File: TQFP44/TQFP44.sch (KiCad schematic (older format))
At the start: 6 parts, among them J1 Conn_01x22, J2 Conn_01x22, J3 Conn_02x22_Counter_Clockwise, J4 Conn_02x22_Counter_Clockwise, J5 Conn_02x22_Counter_Clockwise, J6 Conn_01x06

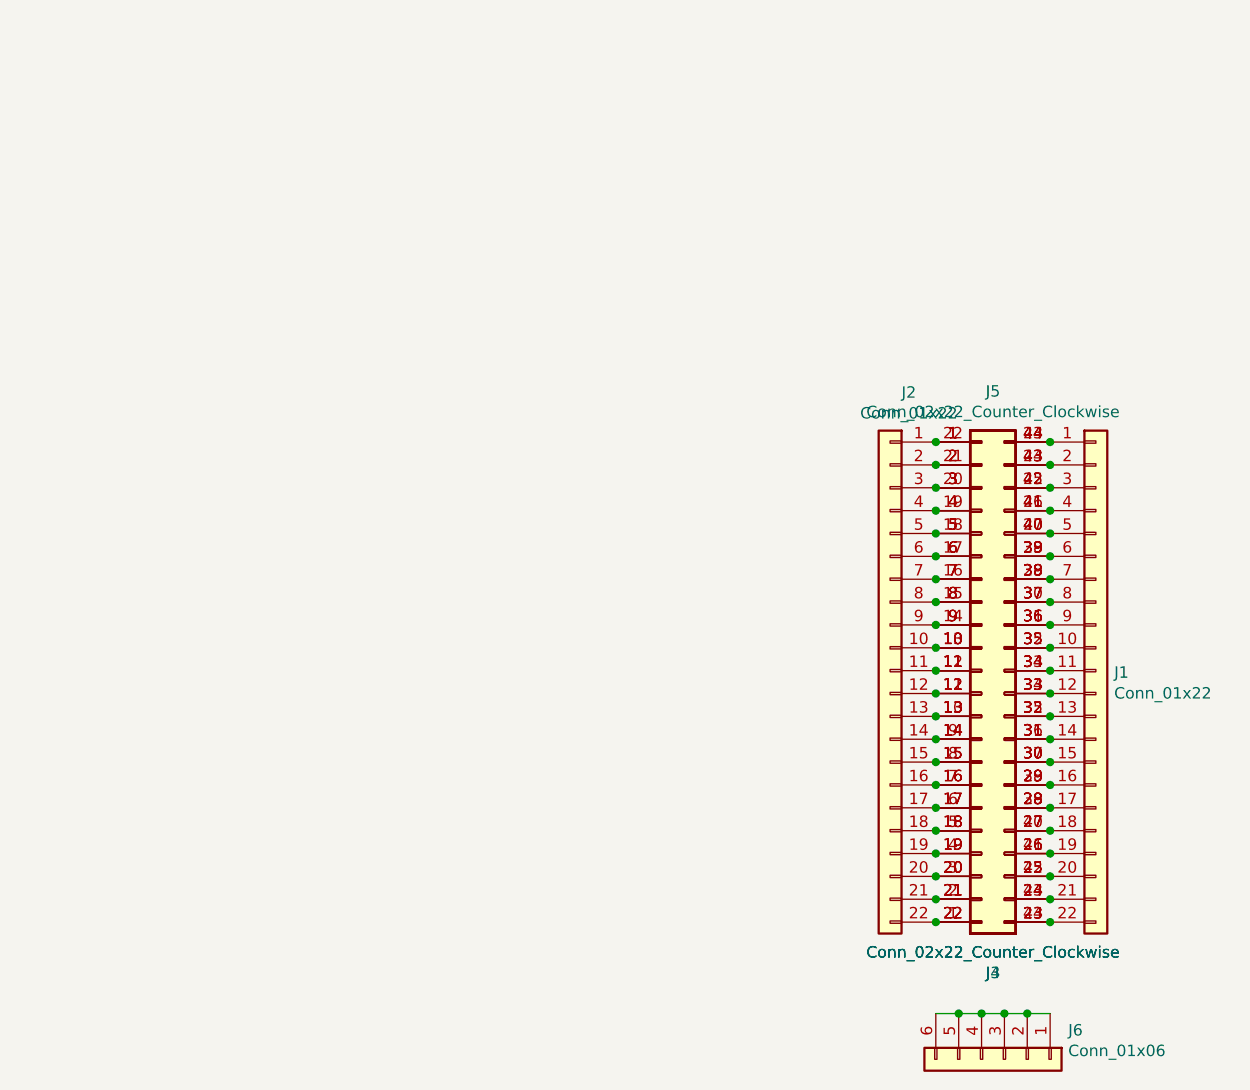
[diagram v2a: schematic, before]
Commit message: USB, SD and CR Cells Added
MicroSD, MicroUSB, MiniUSB, USB-C, CR1220, CR2032 added as well as all schematics page sizes optimised
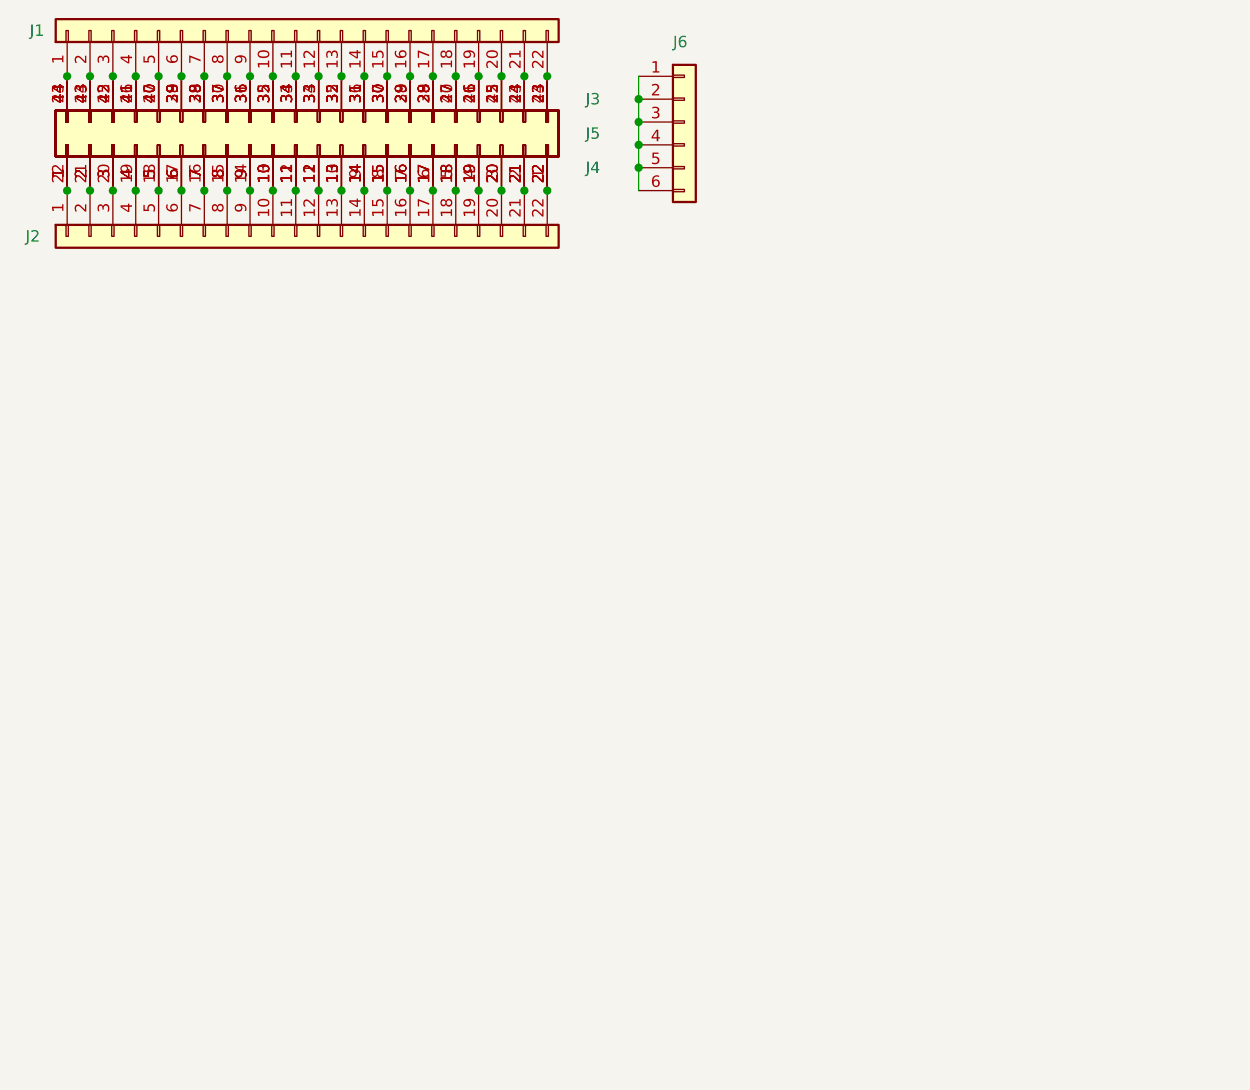
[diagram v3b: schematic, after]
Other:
- moved on the sheet: J1, J2, J3, J4, J5, J6
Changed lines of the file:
@@
 EELAYER 29 0
 EELAYER END
-$Descr A4 11693 8268
+$Descr User 5197 4016
 encoding utf-8
 Sheet 1 1
-Title ""
-Date ""
-Rev ""
-Comp ""
-Comment1 ""
-Comment2 ""
-Comment3 ""
-Comment4 ""
+Title "TQFP44 to DIP44 Breakout Board"
+Date "2019-07-04"
+Rev "1"
+Comp "SirBoard"
+Comment1 "TQFP44 P = 0.8mm"
+Comment2 "QFN44 P = 0.5mm"
+Comment3 "TSSOP44 P = 0.65mm"
+Comment4 "DIP44 P = 2.54mm"
 $EndDescr
 $Comp
 L Connector_Generic:Conn_01x22 J1
 U 1 1 5D21790C
-P 5800 3850
-F 0 "J1" H 5880 3842 50  0000 L CNN
-F 1 "Conn_01x22" H 5880 3751 50  0000 L CNN
-F 2 "Connector_PinHeader_2.54mm:PinHeader_1x22_P2.54mm_Vertical" H 5800 3850 50  0001 C CNN
-F 3 "~" H 5800 3850 50  0001 C CNN
-	1    5800 3850
-	1    0    0    -1
+P 2300 1050
+F 0 "J1" V 2300 2150 50  0000 L CNN
+F 1 "Conn_01x22" H 2380 951 50  0001 L CNN
+F 2 "Connector_PinHeader_2.54mm:PinHeader_1x22_P2.54mm_Vertical" H 2300 1050 50  0001 C CNN
+F 3 "~" H 2300 1050 50  0001 C CNN
+	1    2300 1050
+	0    -1   -1   0
 $EndComp
 $Comp
 L Connector_Generic:Conn_01x22 J2
 U 1 1 5D21CCC0
-P 4900 3850
-F 0 "J2" H 4818 5067 50  0000 C CNN
-F 1 "Conn_01x22" H 4818 4976 50  0000 C CNN
-F 2 "Connector_PinHeader_2.54mm:PinHeader_1x22_P2.54mm_Vertical" H 4900 3850 50  0001 C CNN
-F 3 "~" H 4900 3850 50  0001 C CNN
-	1    4900 3850
-	-1   0    0    -1
+P 2300 1950
+F 0 "J2" V 2300 3100 50  0000 C CNN
+F 1 "Conn_01x22" H 2218 3076 50  0001 C CNN
+F 2 "Connector_PinHeader_2.54mm:PinHeader_1x22_P2.54mm_Vertical" H 2300 1950 50  0001 C CNN
+F 3 "~" H 2300 1950 50  0001 C CNN
+	1    2300 1950
+	0    -1   1    0
 $EndComp
 $Comp
 L Connector_Generic:Conn_02x22_Counter_Clockwise J5
 U 1 1 5D30EF53
-P 5300 3950
-F 0 "J5" H 5350 2628 50  0000 C CNN
-F 1 "Conn_02x22_Counter_Clockwise" H 5350 2718 50  0000 C CNN
-F 2 "Package_QFP:TQFP-44_10x10mm_P0.8mm" H 5300 3950 50  0001 C CNN
-F 3 "~" H 5300 3950 50  0001 C CNN
-	1    5300 3950
-	1    0    0    1
+P 2400 1550
+F 0 "J5" V 2450 2750 50  0000 C CNN
+F 1 "Conn_02x22_Counter_Clockwise" H 2450 318 50  0001 C CNN
+F 2 "Package_QFP:TQFP-44_10x10mm_P0.8mm" H 2400 1550 50  0001 C CNN
+F 3 "~" H 2400 1550 50  0001 C CNN
+	1    2400 1550
+	0    1    -1   0
 $EndComp
 $Comp
 L Connector_Generic:Conn_02x22_Counter_Clockwise J3
 U 1 1 5D2DB143
-P 5300 3850
-F 0 "J3" H 5350 2528 50  0000 C CNN
-F 1 "Conn_02x22_Counter_Clockwise" H 5350 2618 50  0000 C CNN
-F 2 "Package_QFP:TQFP-44_10x10mm_P0.8mm" H 5300 3850 50  0001 C CNN
-F 3 "~" H 5300 3850 50  0001 C CNN
-	1    5300 3850
-	1    0    0    -1
+P 2300 1550
+F 0 "J3" V 2500 250 50  0000 C CNN
+F 1 "Conn_02x22_Counter_Clockwise" H 2350 318 50  0001 C CNN
+F 2 "Package_QFP:TQFP-44_10x10mm_P0.8mm" H 2300 1550 50  0001 C CNN
+F 3 "~" H 2300 1550 50  0001 C CNN
+	1    2300 1550
+	0    -1   -1   0
 $EndComp
-Connection ~ 5100 2850
-Connection ~ 5100 2950
-Connection ~ 5100 3050
-Connection ~ 5100 3150
-Connection ~ 5100 3250
-Connection ~ 5100 3350
-Connection ~ 5100 3450
-Connection ~ 5100 3550
-Connection ~ 5100 3650
-Connection ~ 5100 3750
-Connection ~ 5100 3850
-Connection ~ 5100 3950
-Connection ~ 5100 4050
-Connection ~ 5100 4150
-Connection ~ 5100 4250
-Connection ~ 5100 4350
-Connection ~ 5100 4450
-Connection ~ 5100 4550
-Connection ~ 5100 4650
-Connection ~ 5100 4750
-Connection ~ 5100 4850
-Connection ~ 5100 4950
-Connection ~ 5600 2850
-Connection ~ 5600 2950
-Connection ~ 5600 3050
-Connection ~ 5600 3150
-Connection ~ 5600 3250
-Connection ~ 5600 3350
-Connection ~ 5600 3450
-Connection ~ 5600 3550
-Connection ~ 5600 3650
-Connection ~ 5600 3750
-Connection ~ 5600 3850
-Connection ~ 5600 3950
-Connection ~ 5600 4050
-Connection ~ 5600 4150
-Connection ~ 5600 4250
-Connection ~ 5600 4350
-Connection ~ 5600 4450
-Connection ~ 5600 4550
-Connection ~ 5600 4650
-Connection ~ 5600 4750
-Connection ~ 5600 4850
-Connection ~ 5600 4950
+Connection ~ 1300 1750
+Connection ~ 1400 1750
+Connection ~ 1500 1750
+Connection ~ 1600 1750
+Connection ~ 1700 1750
+Connection ~ 1800 1750
+Connection ~ 1900 1750
+Connection ~ 2000 1750
+Connection ~ 2100 1750
+Connection ~ 2200 1750
+Connection ~ 2300 1750
+Connection ~ 2400 1750
+Connection ~ 2500 1750
+Connection ~ 2600 1750
+Connection ~ 2700 1750
+Connection ~ 2800 1750
+Connection ~ 2900 1750
+Connection ~ 3000 1750
+Connection ~ 3100 1750
+Connection ~ 3200 1750
+Connection ~ 3300 1750
+Connection ~ 3400 1750
+Connection ~ 1300 1250
+Connection ~ 1400 1250
+Connection ~ 1500 1250
+Connection ~ 1600 1250
+Connection ~ 1700 1250
+Connection ~ 1800 1250
+Connection ~ 1900 1250
+Connection ~ 2000 1250
+Connection ~ 2100 1250
+Connection ~ 2200 1250
+Connection ~ 2300 1250
+Connection ~ 2400 1250
+Connection ~ 2500 1250
+Connection ~ 2600 1250
+Connection ~ 2700 1250
+Connection ~ 2800 1250
+Connection ~ 2900 1250
+Connection ~ 3000 1250
+Connection ~ 3100 1250
+Connection ~ 3200 1250
+Connection ~ 3300 1250
+Connection ~ 3400 1250
 $Comp
 L Connector_Generic:Conn_01x06 J6
 U 1 1 5D343C09
-P 5400 5550
-F 0 "J6" V 5273 5829 50  0000 L CNN
-F 1 "Conn_01x06" V 5363 5829 50  0000 L CNN
-F 2 "Connector_PinHeader_2.54mm:PinHeader_1x06_P2.54mm_Horizontal" H 5400 5550 50  0001 C CNN
-F 3 "~" H 5400 5550 50  0001 C CNN
-	1    5400 5550
-	0    1    1    0
+P 4000 1450
+F 0 "J6" H 3950 1800 50  0000 L CNN
+F 1 "Conn_01x06" V 3963 1729 50  0001 L CNN
+F 2 "Connector_PinHeader_2.54mm:PinHeader_1x06_P2.54mm_Horizontal" H 4000 1450 50  0001 C CNN
+F 3 "~" H 4000 1450 50  0001 C CNN
+	1    4000 1450
+	1    0    0    -1
 $EndComp
-Connection ~ 5400 5350
+Connection ~ 3800 1450
 Wire Wire Line
-	5400 5350 5500 5350
-Connection ~ 5500 5350
+	3800 1450 3800 1350
+Connection ~ 3800 1350
 Wire Wire Line
-	5500 5350 5600 5350
+	3800 1350 3800 1250
 Wire Wire Line
-	5100 5350 5200 5350
-Connection ~ 5200 5350
+	3800 1750 3800 1650
+Connection ~ 3800 1650
 Wire Wire Line
-	5200 5350 5300 5350
-Connection ~ 5300 5350
+	3800 1650 3800 1550
+Connection ~ 3800 1550
 Wire Wire Line
-	5300 5350 5400 5350
+	3800 1550 3800 1450
 $Comp
 L Connector_Generic:Conn_02x22_Counter_Clockwise J4
 U 1 1 5D472302
-P 5300 3850
-F 0 "J4" H 5350 2528 50  0000 C CNN
-F 1 "Conn_02x22_Counter_Clockwise" H 5350 2618 50  0000 C CNN
-F 2 "Package_DFN_QFN:QFN-44-1EP_7x7mm_P0.5mm_EP5.15x5.15mm" H 5300 3850 50  0001 C CNN
-F 3 "~" H 5300 3850 50  0001 C CNN
-	1    5300 3850
-	1    0    0    -1
+P 2300 1550
+F 0 "J4" V 2200 250 50  0000 C CNN
+F 1 "Conn_02x22_Counter_Clockwise" H 2350 318 50  0001 C CNN
+F 2 "Package_DFN_QFN:QFN-44-1EP_7x7mm_P0.5mm_EP5.15x5.15mm" H 2300 1550 50  0001 C CNN
+F 3 "~" H 2300 1550 50  0001 C CNN
+	1    2300 1550
+	0    -1   -1   0
 $EndComp
 $EndSCHEMATC
